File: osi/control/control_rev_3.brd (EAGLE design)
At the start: 25.4 x 25.4 mm, 13 parts, among them IC1 UA7805CKCS, IC2 MCP1702

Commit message: furby board production
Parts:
- removed D1: (no value), SparkFun:DIODE-1N4148
- removed F1: PTCPTH, SparkFun_mod:PTC
- removed IC1: UA7805CKCS, SparkFun:TO-220-ALT
- removed IC2: MCP1702, adafruit:TO92-INLINE
- removed LED1: (no value), adafruit:LED3MM
- removed R1: 1k, adafruit:0204/5
- removed U$1: 2.1MMJACKTHM, adafruit:PJ-102A
- removed U$2: (no value), DC_SYM:DC_POS_CTR
- removed U$3: (no value), DC_SYM:DC_POS_CTR-BOTTOM
- added C3: 0.1uF, rcl-ez:C025-025X050
- added JP1: (no value), adafruit_mod:1X03
- added MTR1, MTR2: TERMINAL, _my-parts:TERMINAL_3
- added TRACKS: L293D, texas:DIL16
- C1: value 0.33uF -> 100uF/16V; device adafruit:C025-024X044 -> rcl-ez:E2,5-6
- C2: value 1uF -> 100uF/16V; device adafruit:C025-024X044 -> rcl-ez:E2,5-6
- moved C2 13.4 mm to (22.5, 18.7)
- moved C1 10.3 mm to (22.6, 2.92), turned to 270 degrees
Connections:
- net D10 renamed D7-D13
- net D11 renamed A1-A6
- net D12 renamed A2-A7
- removed net A0: JP5.2
- removed net A1: JP5.1
- removed net A2: JP6.1
- removed net A3: JP6.2
- removed net A7: JP5.3
- removed net D13: JP5.4
- new net A3-A0: JP5.4, TRACKS.10
- new net D2-D8: JP6.1, TRACKS.1
- new net D3-D9: JP5.3, TRACKS.15
- new net D4-D12: JP6.2, TRACKS.9
- new net D5-D10: JP5.2, TRACKS.2
- new net D6-D11: JP5.1, TRACKS.7
- new net N$4: MTR2.P$3, TRACKS.11
- new net N$8: C2.+, JP1.2, TRACKS.8
- net +3V3: no longer IC2.3
- net +5V: now also C1.+, C3.1, JP1.1, TRACKS.16; no longer C2.1, IC1.OUT, IC2.2, LED1.A
- net GND: now also C1.-, C2.-, C3.2, MTR1.P$2, MTR2.P$2, TRACKS.12, TRACKS.13, TRACKS.4, TRACKS.5; no longer C1.2, C2.2, IC1.GND, IC2.1, R1.2, U$1.RING
- net N$1: now also MTR1.P$1, TRACKS.3; no longer F1.P$1, U$1.TIP
- net N$2: now also MTR2.P$1, TRACKS.14; no longer LED1.K, R1.1
- net N$3: now also MTR1.P$3, TRACKS.6; no longer D1.A, F1.P$2
- net V+: now also JP1.3; no longer C1.1, D1.C, IC1.IN
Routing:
- net V+: track 53.1 -> 11.3 mm
- net D6-D11: track 0.00 -> 34.1 mm
- net D4-D12: track 0.00 -> 22.7 mm
- net D5-D10: track 0.00 -> 21.4 mm
- net D3-D9: track 0.00 -> 15.1 mm
- net A3-A0: track 0.00 -> 13.8 mm
- net N$8: track 0.00 -> 13.6 mm
- net N$3: track 2.41 -> 14.9 mm
- net +3V3: track 7.07 -> 0.00 mm
- net +5V: track 58.4 -> 51.4 mm
- net N$1: track 6.30 -> 13.1 mm
- net N$2: track 2.02 -> 8.30 mm
- net N$4: track 0.00 -> 5.76 mm
- net D2-D8: track 0.00 -> 4.07 mm
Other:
- board size 25.4 x 25.4 mm -> 24.8 x 25.4 mm
- board text added: "100uf"
- board text added: "<-sel->"
- board text added: "Apr 12"
- board text added: "CNTRL"
- board text added: "CTRL"
- board text added: "LM293"
- board text removed: "1.5A"
- board text removed: "1k"
- board text removed: "1uF"
- board text removed: "25V"
- board text removed: "3V: 0.25A"
- board text removed: "5V: 1.5A"
- board text removed: "7-25 VDC"
- board text removed: "Apr 13"
- board text removed: "MCP1702"
- board text removed: "PTC"
- board text removed: "PWR"
- board text removed: "UA7805CKCS"

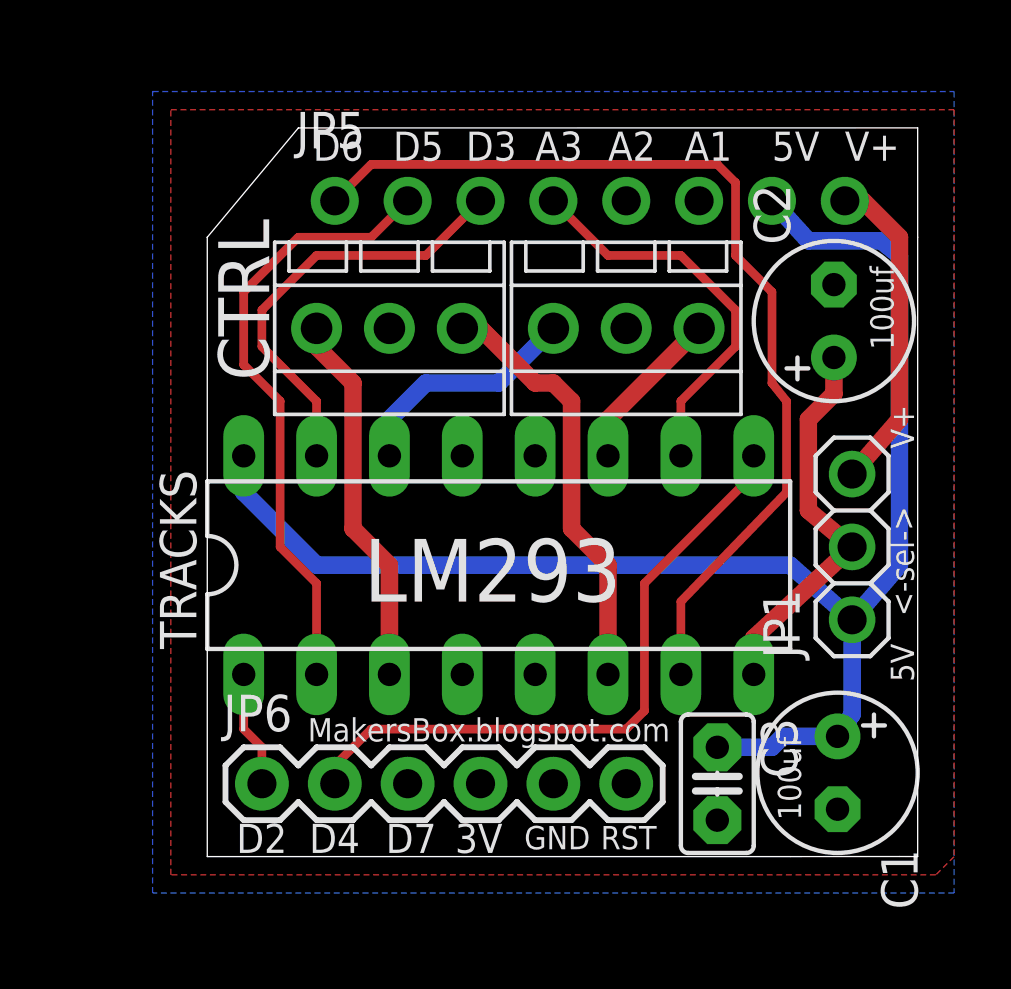
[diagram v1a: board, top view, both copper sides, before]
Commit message: moving headers
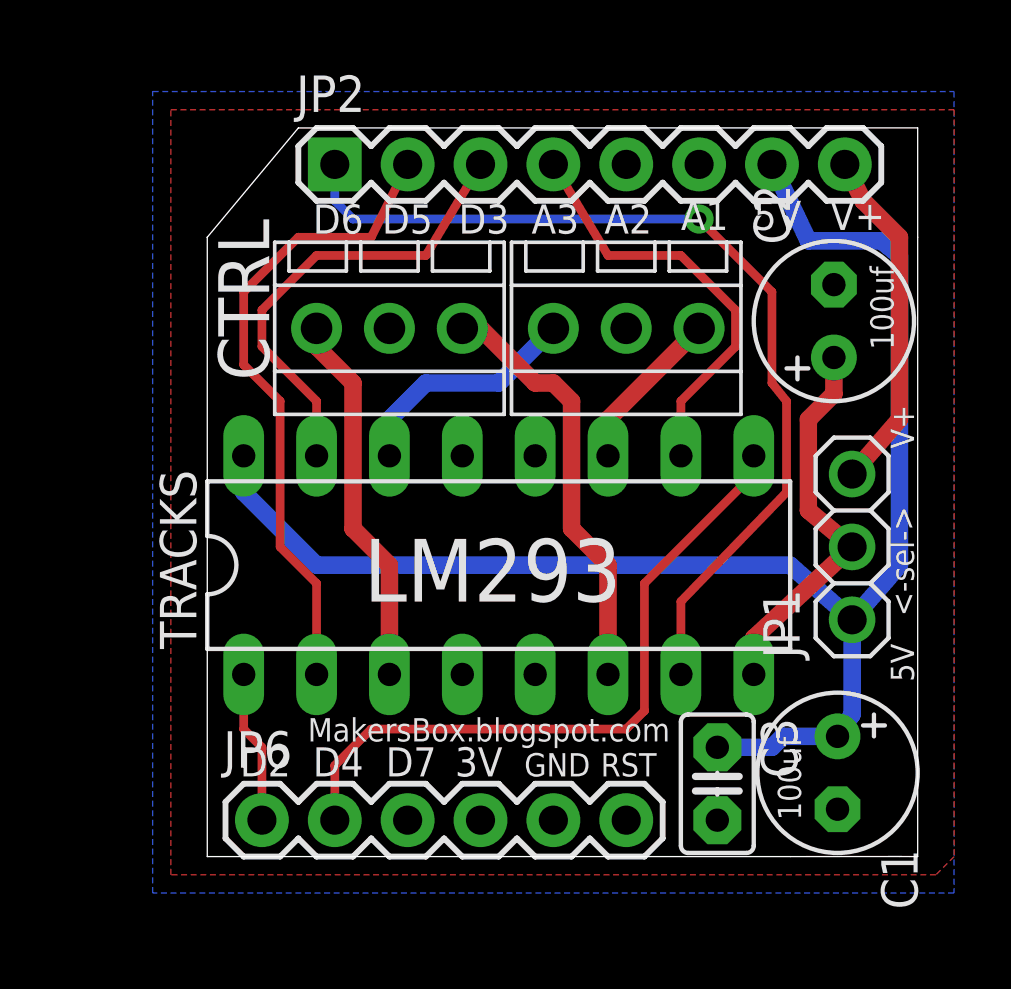
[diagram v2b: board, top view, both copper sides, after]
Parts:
- removed JP5: (no value), SparkFun_mod:1X08
- added JP2: (no value), SparkFun:1X08
- moved JP6 1.27 mm to (2.54, 1.27)
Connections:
- net +5V: now also JP2.7; no longer JP5.7
- net A1-A6: now also JP2.6; no longer JP5.6
- net A2-A7: now also JP2.5; no longer JP5.5
- net A3-A0: now also JP2.4; no longer JP5.4
- net D3-D9: now also JP2.3; no longer JP5.3
- net D5-D10: now also JP2.2; no longer JP5.2
- net D6-D11: now also JP2.1; no longer JP5.1
- net V+: now also JP2.8; no longer JP5.8
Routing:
- net D4-D12: track 22.7 -> 24.0 mm
- net D2-D8: track 4.07 -> 5.34 mm
- net D6-D11: track 34.1 -> 32.8 mm, vias 0 -> 1
- net +5V: track 51.4 -> 52.4 mm
- net D5-D10: track 21.4 -> 22.5 mm
- net D3-D9: track 15.1 -> 16.1 mm
- net A3-A0: track 13.8 -> 14.8 mm
- net V+: track 11.3 -> 12.1 mm
